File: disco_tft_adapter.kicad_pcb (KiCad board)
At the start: 4 copper layers, 127 x 116.1 mm, 22 parts, among them J1 QTH-030-02-L-D-A, J2 F31L-1A7H1-11030

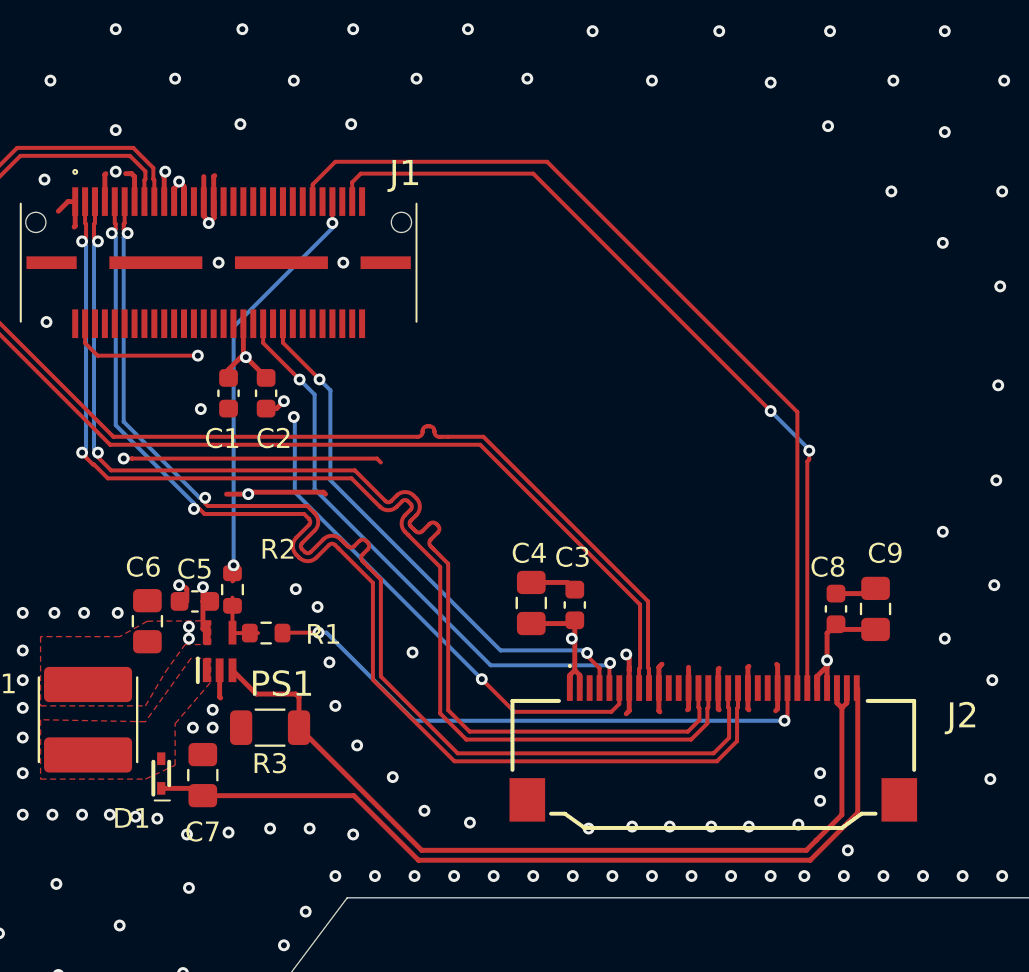
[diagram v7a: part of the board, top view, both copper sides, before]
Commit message: [all] add test points using a custom footprint
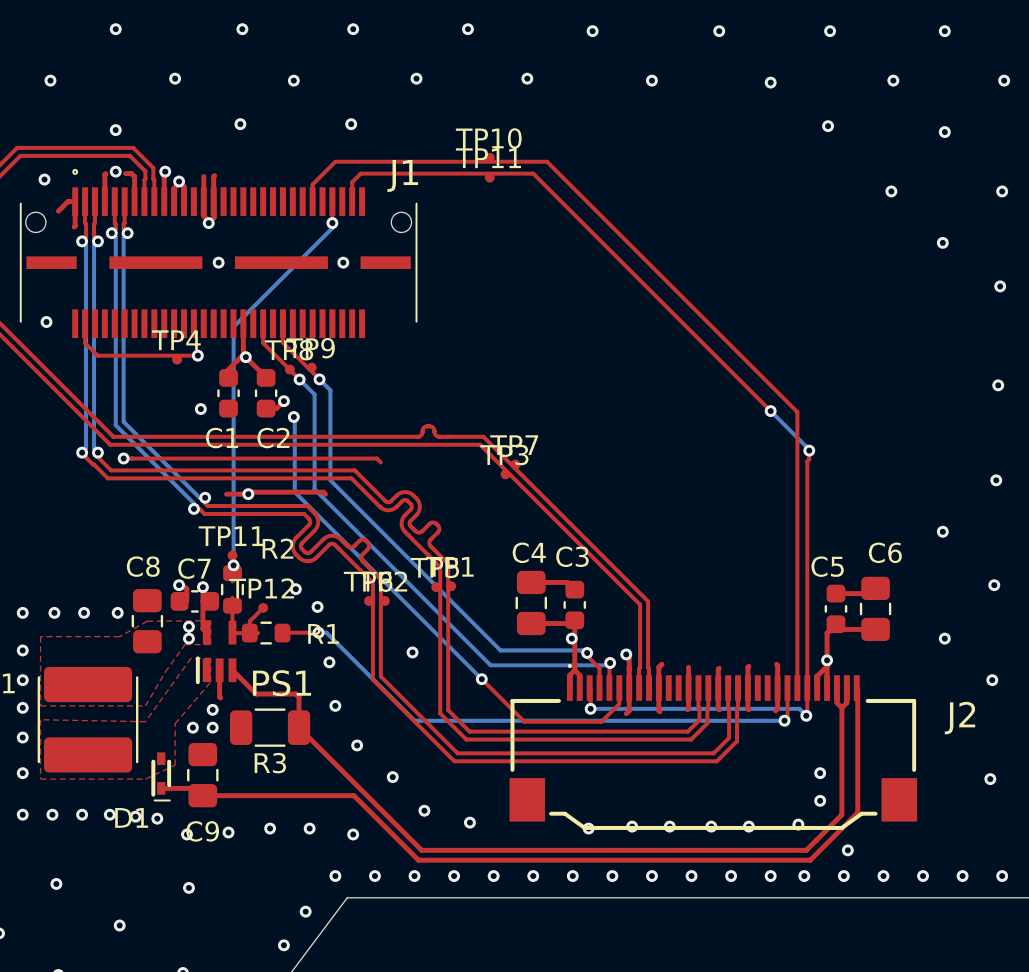
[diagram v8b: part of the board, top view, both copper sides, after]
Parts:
- added TP1: TestPoint_Alt, aa_prj:TestPoint_TP_D0.5mm, F.Cu at (89.5, 112.0)
- added TP10: TestPoint_Alt, aa_prj:TestPoint_TP_D0.5mm, F.Cu at (91.4, 90.3)
- added TP11: TestPoint_Alt, aa_prj:TestPoint_TP_D0.5mm, F.Cu at (91.4, 91.3)
- added TP11: TestPoint_Alt, aa_prj:TestPoint_TP_D0.5mm, F.Cu at (78.4, 110.4)
- added TP12: TestPoint_Alt, aa_prj:TestPoint_TP_D0.5mm, F.Cu at (80.0, 113.0)
- added TP2: TestPoint_Alt, aa_prj:TestPoint_TP_D0.5mm, F.Cu at (86.1, 112.7)
- added TP3: TestPoint_Alt, aa_prj:TestPoint_TP_D0.5mm, F.Cu at (92.2, 106.3)
- added TP4: TestPoint_Alt, aa_prj:TestPoint_TP_D0.5mm, F.Cu at (75.6, 100.5)
- added TP5: TestPoint_Alt, aa_prj:TestPoint_TP_D0.5mm, F.Cu at (88.7, 112.0)
- added TP6: TestPoint_Alt, aa_prj:TestPoint_TP_D0.5mm, F.Cu at (85.3, 112.7)
- added TP7: TestPoint_Alt, aa_prj:TestPoint_TP_D0.5mm, F.Cu at (92.7, 105.8)
- added TP8: TestPoint_Alt, aa_prj:TestPoint_TP_D0.5mm, F.Cu at (81.3, 101.0)
- added TP9: TestPoint_Alt, aa_prj:TestPoint_TP_D0.5mm, F.Cu at (82.4, 100.9)
- renumbered C8 to C5, C9 to C6, C5 to C7, C6 to C8, C7 to C9
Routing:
- net /RST: track 42.1 -> 55.7 mm, vias 2 -> 4
- net Net-(PS1-CTRL): track 3.07 -> 4.62 mm
